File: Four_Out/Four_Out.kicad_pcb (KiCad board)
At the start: 2 copper layers, 60.7 x 66.3 mm, 25 parts, among them J1 String1, J2 String2, J3 String3, J4 String4, J5 Power In, J6 Expansion Header, U1 74HC125

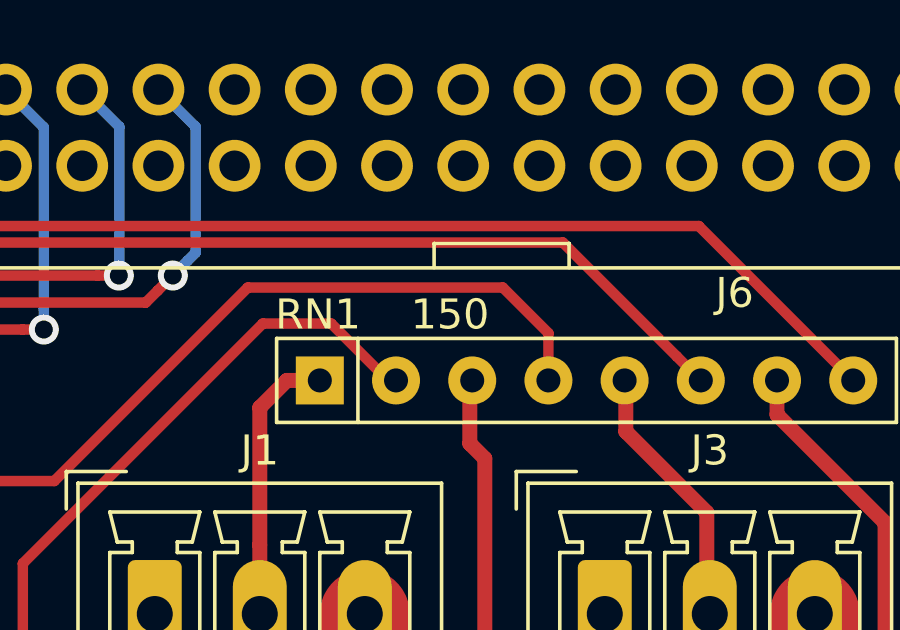
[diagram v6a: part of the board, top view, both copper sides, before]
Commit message: Updated Pixel Pixel resistor packs to 33ohms
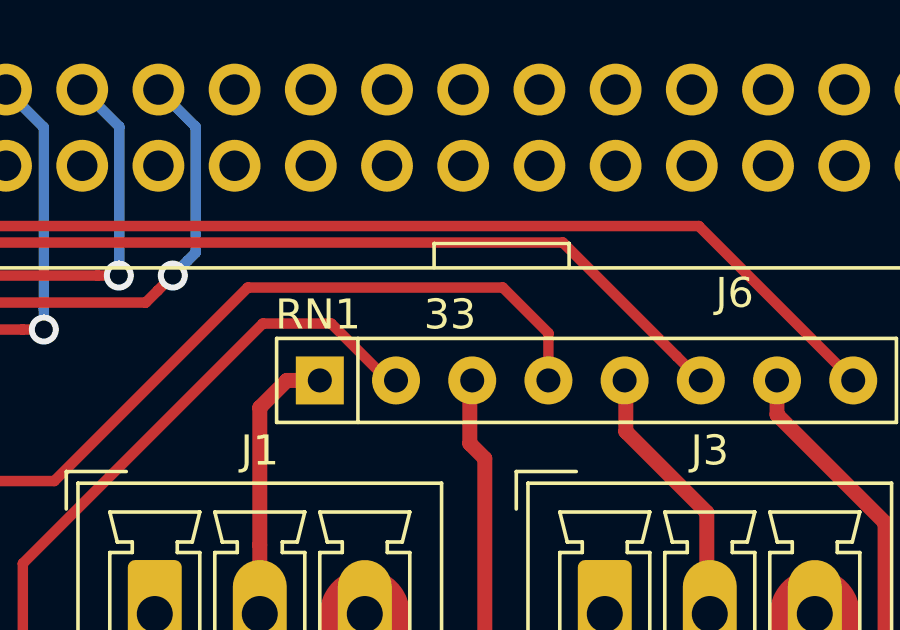
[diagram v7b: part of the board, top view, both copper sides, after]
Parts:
- RN1: value 150 -> 33

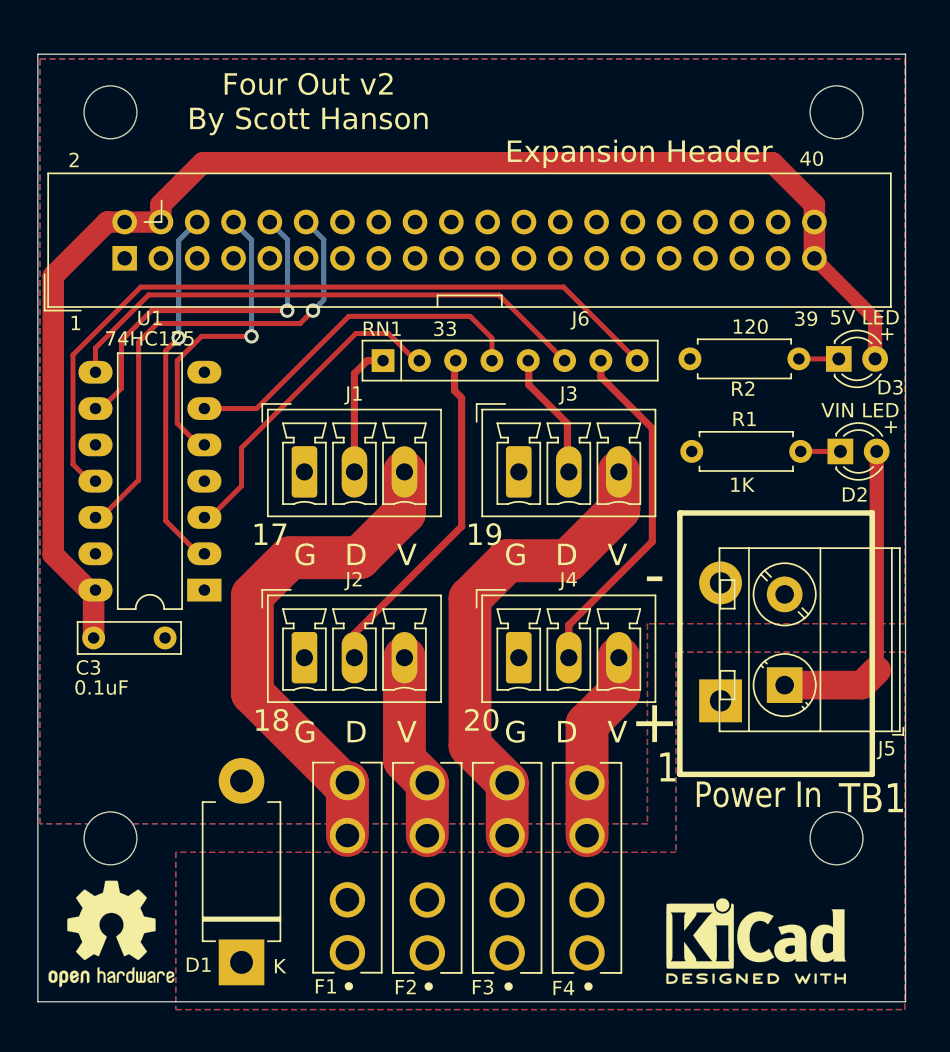
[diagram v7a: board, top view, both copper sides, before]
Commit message: added v4 Header
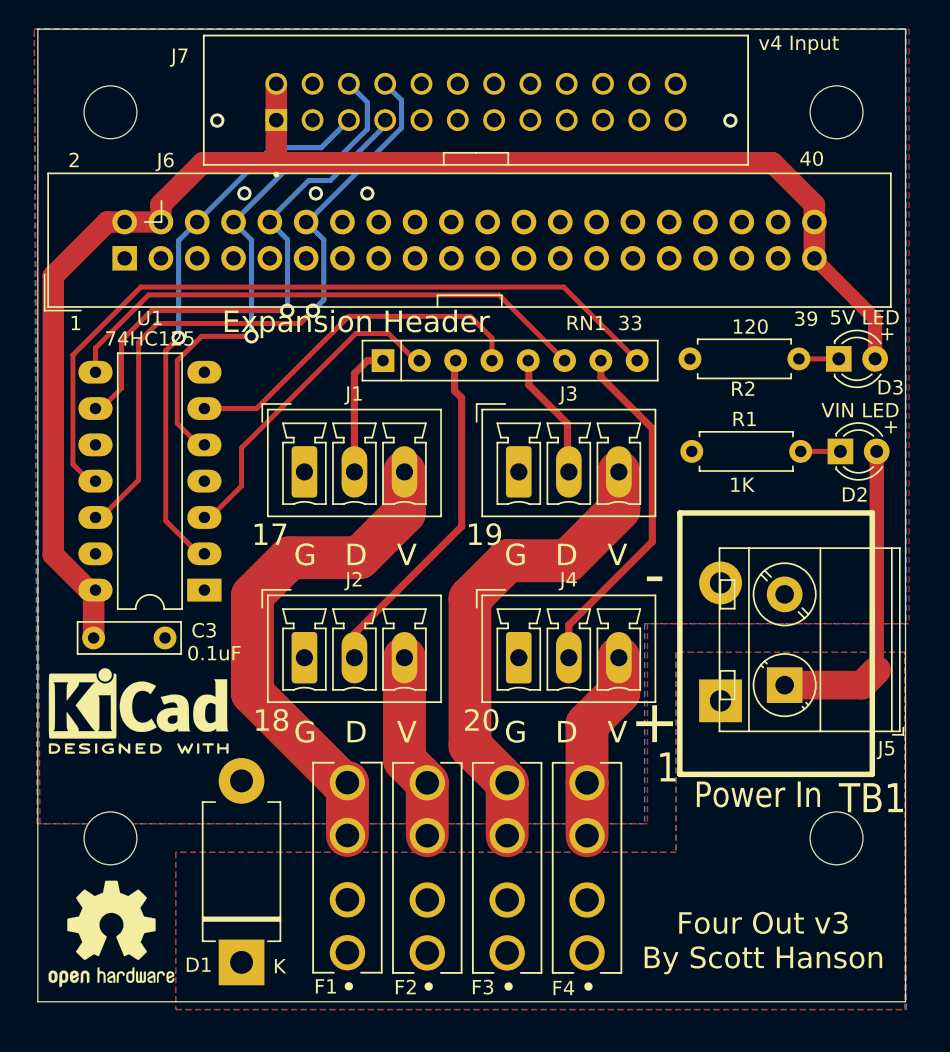
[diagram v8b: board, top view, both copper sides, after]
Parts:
- added J7: v4 Input, 302-S241:OST_302-S241, F.Cu at (98.3, 90.7)
- moved REF** 46.1 mm to (74.7, 133.3)
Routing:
- net OUT18: track 21.3 -> 37.1 mm
- net OUT17: track 25.5 -> 39.0 mm
- net OUT20: track 33.9 -> 46.8 mm
- net OUT19: track 24.9 -> 36.3 mm
- net +5V: track 97.9 -> 103.4 mm
- net GND: vias 0 -> 5
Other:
- board size 60.7 x 66.3 mm -> 60.7 x 68.1 mm
- board text added: "Four Out v3 By Scott Hanson"
- board text removed: "Four Out v2 By Scott Hanson"
